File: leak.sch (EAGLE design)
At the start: 5 parts, among them IC1 74HC595D

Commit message: modifications
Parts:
- added C1, C2, C3, C4, C5, C6, C7, C8: 1uF, rcl:C-EUC0603
- added IC2, IC3: 74HC595D, 74xx-eu:74HC595D
- added U$10, U$5, U$6, U$7, U$8, U$9: AD5270MSOP10, untitled:AD5270MSOP10
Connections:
- new net +2V5: U$1.VDD, U$10.VDD, U$2.VDD, U$5.VDD, U$6.VDD, U$7.VDD, U$8.VDD, U$9.VDD
- new net -2V5: U$1.VSS, U$10.VSS, U$2.VSS, U$5.VSS, U$6.VSS, U$7.VSS, U$8.VSS, U$9.VSS
- new net AQA: IC1A.QA, U$2.A
- new net AQB: IC1A.QB, U$1.A
- new net AQC: IC1A.QC, U$5.A
- new net AQD: IC1A.QD, U$6.A
- new net AQE: IC1A.QE, U$7.A
- new net AQF: IC1A.QF, U$8.A
- new net AQG: IC1A.QG, U$9.A
- new net AQH: IC1A.QH, U$10.A
- new net CSA: IC2A.QA, U$2.NSYNC
- new net CSB: IC2A.QB, U$1.NSYNC
- new net CSC: IC2A.QC, U$5.NSYNC
- new net CSD: IC2A.QD, U$6.NSYNC
- new net CSE: IC2A.QE, U$7.NSYNC
- new net CSF: IC2A.QF, U$8.NSYNC
- new net CSG: IC2A.QG, U$9.NSYNC
- new net CSH: IC2A.QH, U$10.NSYNC
- new net GND: C1.1, C2.1, C3.1, C4.1, C5.1, C6.1, C7.1, C8.1, U$1.GND, U$10.GND, U$2.GND, U$5.GND, U$6.GND, U$7.GND, U$8.GND, U$9.GND
- new net MISO: U$1.SDO, U$10.SDO, U$2.SDO, U$5.SDO, U$6.SDO, U$7.SDO, U$8.SDO, U$9.SDO
- new net MOSI: U$1.DIN, U$10.DIN, U$2.DIN, U$5.DIN, U$6.DIN, U$7.DIN, U$8.DIN, U$9.DIN
- new net N$11: C4.2, U$6.CAP
- new net N$14: C5.2, U$7.CAP
- new net N$17: C6.2, U$8.CAP
- new net N$20: C7.2, U$9.CAP
- new net N$23: C8.2, U$10.CAP
- new net N$3: C2.2, U$1.CAP
- new net N$5: C1.2, U$2.CAP
- new net N$8: C3.2, U$5.CAP
- new net SCLK: U$1.SCLK, U$10.SCLK, U$2.SCLK, U$5.SCLK, U$6.SCLK, U$7.SCLK, U$8.SCLK, U$9.SCLK
- new net W: U$1.W, U$10.W, U$2.W, U$5.W, U$6.W, U$7.W, U$8.W, U$9.W
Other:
- moved on the sheet: IC1, U$1, U$3

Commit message: few more connections
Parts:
- removed C8: 1uF, rcl:C-EUC0603
- removed IC3: 74HC595D, 74xx-eu:74HC595D
- removed U$1, U$10, U$2, U$5, U$6, U$7, U$8, U$9: AD5270MSOP10, untitled:AD5270MSOP10
- removed U$3: AD5231, untitled:AD5231
- removed U$4: ADG621, untitled:ADG621
- added ICA, ICB, ICC, ICD, ICE, ICF, ICG: AD5270MSOP10, untitled:AD5270MSOP10
- added ICPOW: AD5231, untitled:AD5231
- added ICSW: ADG621, untitled:ADG621
- added JP1: (no value), pinhead:PINHD-1X3
- added JP4: (no value), pinhead:PINHD-1X6
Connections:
- removed net N$23: C8.2, U$10.CAP
- new net +5V: ICSW.VDD, JP1.1
- new net -5V: ICSW.VSS, JP1.3
- new net CS_CS: IC2A.RCK, JP4.2
- new net CS_IN: IC1A.RCK, JP4.1
- new net LVLA: ICPOW.A, ICSW.D1
- new net LVLB: ICPOW.B, ICSW.D2
- new net LVLW: ICPOW.W
- new net O1: ICPOW.O1, ICSW.IN1
- new net O2: ICPOW.O2, ICSW.IN2
- new net RESET: IC1A.SCL, IC2A.SCL
- net +2V5: now also IC1P.VCC, IC2P.VCC, ICA.VDD, ICB.VDD, ICC.VDD, ICD.VDD, ICE.VDD, ICF.VDD, ICG.VDD, ICPOW.NPR, ICPOW.NWP, ICPOW.VDD, ICSW.S2; no longer U$1.VDD, U$10.VDD, U$2.VDD, U$5.VDD, U$6.VDD, U$7.VDD, U$8.VDD, U$9.VDD
- net -2V5: now also ICA.VSS, ICB.VSS, ICC.VSS, ICD.VSS, ICE.VSS, ICF.VSS, ICG.VSS, ICPOW.T, ICPOW.VSS, ICSW.S1; no longer U$1.VSS, U$10.VSS, U$2.VSS, U$5.VSS, U$6.VSS, U$7.VSS, U$8.VSS, U$9.VSS
- net AQA: now also ICA.A; no longer U$2.A
- net AQB: now also ICB.A; no longer U$1.A
- net AQC: now also ICC.A; no longer U$5.A
- net AQD: now also ICD.A; no longer U$6.A
- net AQE: now also ICE.A; no longer U$7.A
- net AQF: now also ICF.A; no longer U$8.A
- net AQG: now also ICG.A; no longer U$9.A
- net AQH: no longer U$10.A
- net CSA: now also ICA.NSYNC; no longer U$2.NSYNC
- net CSB: now also ICB.NSYNC; no longer U$1.NSYNC
- net CSC: now also ICC.NSYNC; no longer U$5.NSYNC
- net CSD: now also ICD.NSYNC; no longer U$6.NSYNC
- net CSE: now also ICE.NSYNC; no longer U$7.NSYNC
- net CSF: now also ICF.NSYNC; no longer U$8.NSYNC
- net CSG: now also ICG.NSYNC; no longer U$9.NSYNC
- net CSH: now also ICPOW.NCS; no longer U$10.NSYNC
- net GND: now also IC1A.G, IC1P.GND, IC2A.G, IC2P.GND, ICA.GND, ICB.GND, ICC.GND, ICD.GND, ICE.GND, ICF.GND, ICG.GND, ICPOW.GND, ICSW.GND, JP1.2, JP4.6; no longer C8.1, U$1.GND, U$10.GND, U$2.GND, U$5.GND, U$6.GND, U$7.GND, U$8.GND, U$9.GND
- net MISO: now also ICA.SDO, ICB.SDO, ICC.SDO, ICD.SDO, ICE.SDO, ICF.SDO, ICG.SDO, ICPOW.SDO, JP4.4; no longer U$1.SDO, U$10.SDO, U$2.SDO, U$5.SDO, U$6.SDO, U$7.SDO, U$8.SDO, U$9.SDO
- net MOSI: now also IC1A.SER, IC2A.SER, ICA.DIN, ICB.DIN, ICC.DIN, ICD.DIN, ICE.DIN, ICF.DIN, ICG.DIN, ICPOW.SDI, JP4.3; no longer U$1.DIN, U$10.DIN, U$2.DIN, U$5.DIN, U$6.DIN, U$7.DIN, U$8.DIN, U$9.DIN
- net N$11: now also ICD.CAP; no longer U$6.CAP
- net N$14: now also ICE.CAP; no longer U$7.CAP
- net N$17: now also ICF.CAP; no longer U$8.CAP
- net N$20: now also ICG.CAP; no longer U$9.CAP
- net N$3: now also ICB.CAP; no longer U$1.CAP
- net N$5: now also ICA.CAP; no longer U$2.CAP
- net N$8: now also ICC.CAP; no longer U$5.CAP
- net SCLK: now also IC1A.SCK, IC2A.SCK, ICA.SCLK, ICB.SCLK, ICC.SCLK, ICD.SCLK, ICE.SCLK, ICF.SCLK, ICG.SCLK, ICPOW.CLK, JP4.5; no longer U$1.SCLK, U$10.SCLK, U$2.SCLK, U$5.SCLK, U$6.SCLK, U$7.SCLK, U$8.SCLK, U$9.SCLK
- net W: now also ICA.W, ICB.W, ICC.W, ICD.W, ICE.W, ICF.W, ICG.W; no longer U$1.W, U$10.W, U$2.W, U$5.W, U$6.W, U$7.W, U$8.W, U$9.W
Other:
- moved on the sheet: C1, C2, C3, C4, C5, C6, C7, IC1, IC1P, IC2

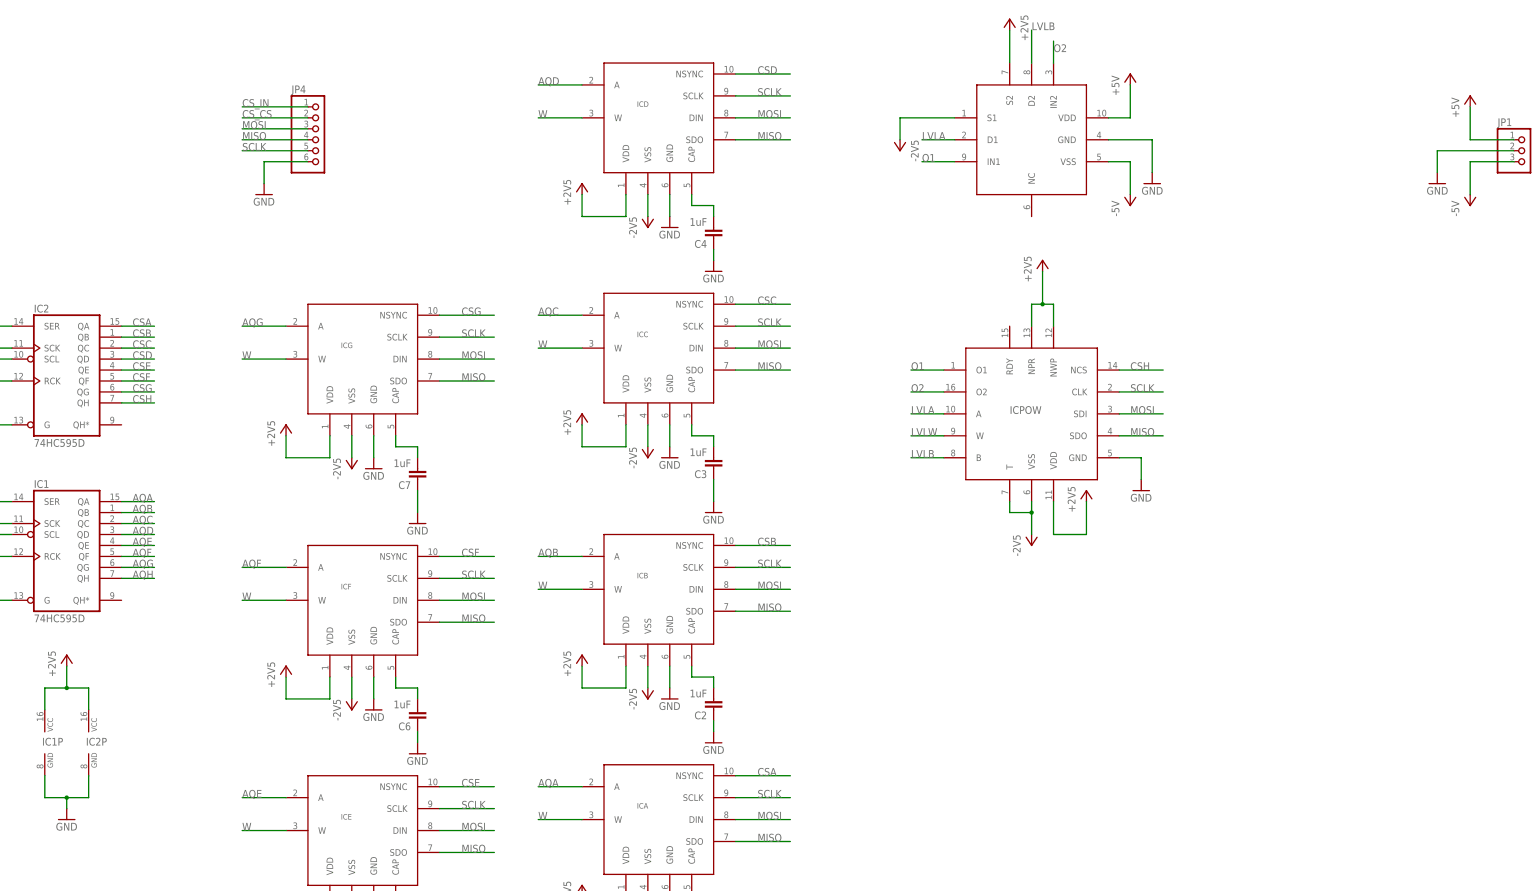
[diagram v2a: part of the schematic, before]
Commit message: added link to a viewer and op amp
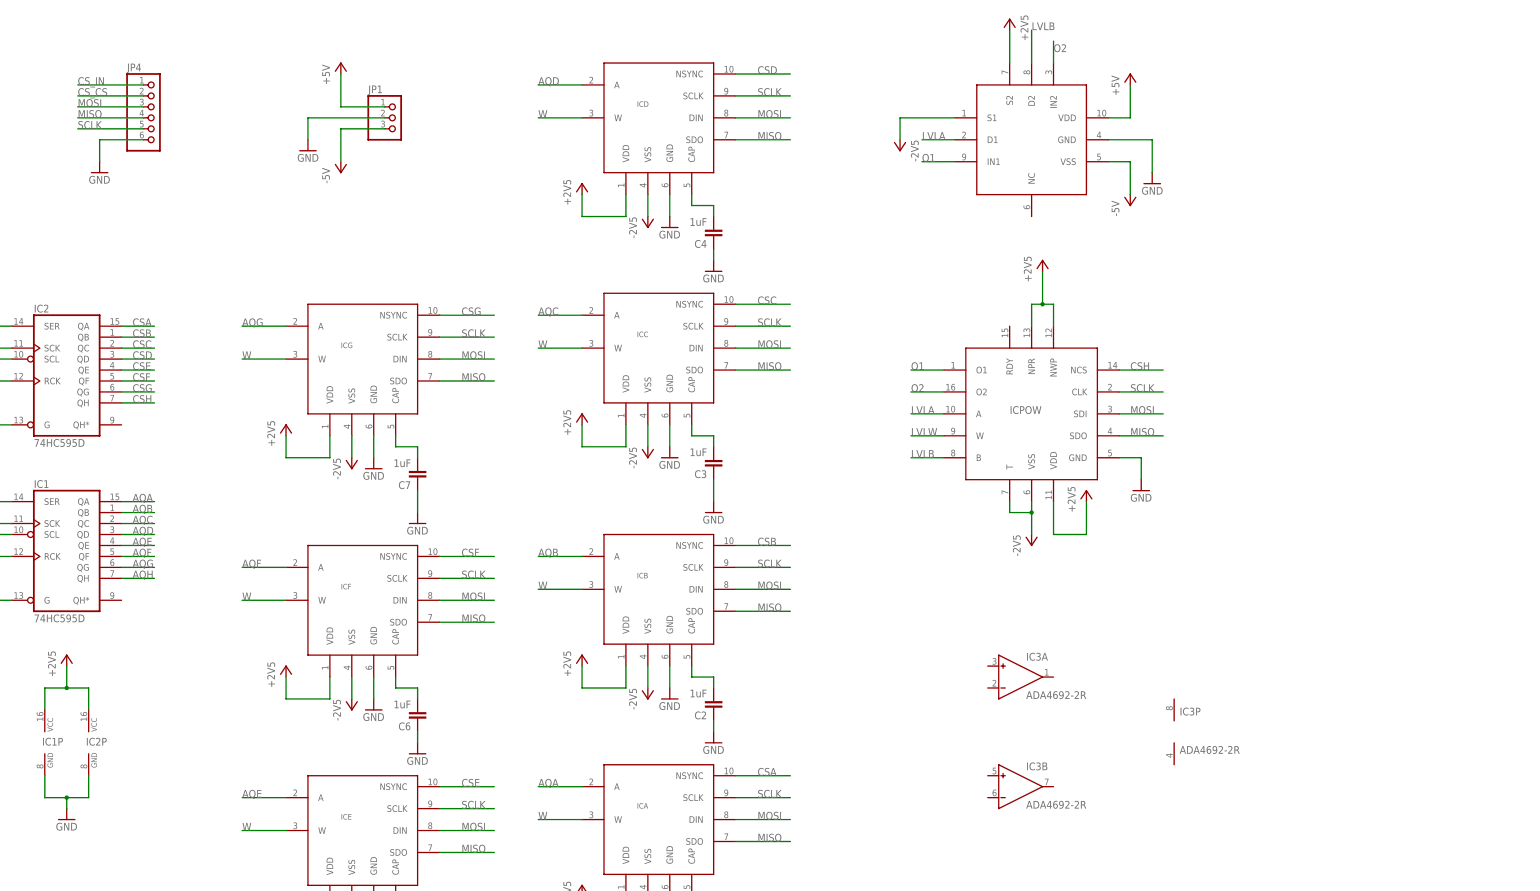
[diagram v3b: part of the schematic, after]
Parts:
- added IC3: ADA4692-2R, analog-devices:ADA4692-2R
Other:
- moved on the sheet: JP1, JP4
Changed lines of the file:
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@@
 <part name="GND21" library="supply1" library_urn="urn:adsk.eagle:library:371" deviceset="GND" device=""/>
 <part name="JP4" library="pinhead" library_urn="urn:adsk.eagle:library:325" deviceset="PINHD-1X6" device="" package3d_urn="urn:adsk.eagle:package:22472/2"/>
+<part name="IC3" library="analog-devices" library_urn="urn:adsk.eagle:library:102" deviceset="ADA4692-2" device="R" package3d_urn="urn:adsk.eagle:package:30987/2"/>
 </parts>
 <sheets>
@@
 <attribute name="VALUE" x="40.64" y="99.06" size="1.778" layer="96" rot="MR0"/>
 </instance>
-<instance part="JP1" gate="A" x="396.24" y="213.36" smashed="yes">
-<attribute name="NAME" x="389.89" y="219.075" size="1.778" layer="95"/>
-<attribute name="VALUE" x="389.89" y="205.74" size="1.778" layer="96"/>
-</instance>
-<instance part="P+1" gate="1" x="383.54" y="226.06" smashed="yes">
-<attribute name="VALUE" x="381" y="220.98" size="1.778" layer="96" rot="R90"/>
-</instance>
-<instance part="P-11" gate="1" x="383.54" y="200.66" smashed="yes">
-<attribute name="VALUE" x="381" y="198.12" size="1.778" layer="96" rot="R90"/>
-</instance>
-<instance part="GND20" gate="1" x="375.92" y="205.74" smashed="yes" rot="MR0">
-<attribute name="VALUE" x="378.46" y="203.2" size="1.778" layer="96" rot="MR0"/>
+<instance part="JP1" gate="A" x="134.62" y="220.98" smashed="yes">
+<attribute name="NAME" x="128.27" y="226.695" size="1.778" layer="95"/>
+<attribute name="VALUE" x="128.27" y="213.36" size="1.778" layer="96"/>
+</instance>
+<instance part="P+1" gate="1" x="121.92" y="233.68" smashed="yes">
+<attribute name="VALUE" x="119.38" y="228.6" size="1.778" layer="96" rot="R90"/>
+</instance>
+<instance part="P-11" gate="1" x="121.92" y="208.28" smashed="yes">
+<attribute name="VALUE" x="119.38" y="205.74" size="1.778" layer="96" rot="R90"/>
+</instance>
+<instance part="GND20" gate="1" x="114.3" y="213.36" smashed="yes" rot="MR0">
+<attribute name="VALUE" x="116.84" y="210.82" size="1.778" layer="96" rot="MR0"/>
 </instance>
 <instance part="P+2" gate="1" x="304.8" y="231.14" smashed="yes">
@@
 <attribute name="VALUE" x="302.26" y="198.12" size="1.778" layer="96" rot="R90"/>
 </instance>
-<instance part="GND21" gate="1" x="104.14" y="203.2" smashed="yes">
-<attribute name="VALUE" x="101.6" y="200.66" size="1.778" layer="96"/>
-</instance>
-<instance part="JP4" gate="A" x="116.84" y="215.9" smashed="yes">
-<attribute name="NAME" x="110.49" y="226.695" size="1.778" layer="95"/>
-<attribute name="VALUE" x="110.49" y="205.74" size="1.778" layer="96"/>
+<instance part="GND21" gate="1" x="66.04" y="208.28" smashed="yes">
+<attribute name="VALUE" x="63.5" y="205.74" size="1.778" layer="96"/>
+</instance>
+<instance part="JP4" gate="A" x="78.74" y="220.98" smashed="yes">
+<attribute name="NAME" x="72.39" y="231.775" size="1.778" layer="95"/>
+<attribute name="VALUE" x="72.39" y="210.82" size="1.778" layer="96"/>
 </instance>
 <instance part="IC2" gate="P" x="63.5" y="76.2" smashed="yes">
 <attribute name="NAME" x="62.865" y="75.565" size="1.778" layer="95"/>
+</instance>
+<instance part="IC3" gate="A" x="276.86" y="91.44" smashed="yes">
+<attribute name="NAME" x="280.67" y="95.25" size="1.778" layer="95"/>
+<attribute name="VALUE" x="280.67" y="86.36" size="1.778" layer="96"/>
+</instance>
+<instance part="IC3" gate="B" x="276.86" y="66.04" smashed="yes">
+<attribute name="NAME" x="280.67" y="69.85" size="1.778" layer="95"/>
+<attribute name="VALUE" x="280.67" y="60.96" size="1.778" layer="96"/>
+</instance>
+<instance part="IC3" gate="P" x="314.96" y="78.74" smashed="yes">
+<attribute name="NAME" x="316.23" y="82.55" size="1.778" layer="95"/>
+<attribute name="VALUE" x="316.23" y="73.66" size="1.778" layer="96"/>
 </instance>
 </instances>
@@
 <segment>
 <pinref part="JP4" gate="A" pin="5"/>
-<wire x1="114.3" y1="213.36" x2="99.06" y2="213.36" width="0.1524" layer="91"/>
-<label x="99.06" y="213.36" size="1.778" layer="95"/>
+<wire x1="76.2" y1="218.44" x2="60.96" y2="218.44" width="0.1524" layer="91"/>
+<label x="60.96" y="218.44" size="1.778" layer="95"/>
 </segment>
 </net>
@@
 <segment>
 <pinref part="JP4" gate="A" pin="3"/>
-<wire x1="114.3" y1="218.44" x2="99.06" y2="218.44" width="0.1524" layer="91"/>
-<label x="99.06" y="218.44" size="1.778" layer="95"/>
+<wire x1="76.2" y1="223.52" x2="60.96" y2="223.52" width="0.1524" layer="91"/>
+<label x="60.96" y="223.52" size="1.778" layer="95"/>
 </segment>
 </net>
@@
 <segment>
 <pinref part="JP4" gate="A" pin="4"/>
-<wire x1="114.3" y1="215.9" x2="99.06" y2="215.9" width="0.1524" layer="91"/>
-<label x="99.06" y="215.9" size="1.778" layer="95"/>
+<wire x1="76.2" y1="220.98" x2="60.96" y2="220.98" width="0.1524" layer="91"/>
+<label x="60.96" y="220.98" size="1.778" layer="95"/>
 </segment>
 </net>
@@
 <segment>
 <pinref part="JP1" gate="A" pin="2"/>
-<wire x1="393.7" y1="213.36" x2="375.92" y2="213.36" width="0.1524" layer="91"/>
-<wire x1="375.92" y1="213.36" x2="375.92" y2="208.28" width="0.1524" layer="91"/>
+<wire x1="132.08" y1="220.98" x2="114.3" y2="220.98" width="0.1524" layer="91"/>
+<wire x1="114.3" y1="220.98" x2="114.3" y2="215.9" width="0.1524" layer="91"/>
 <pinref part="GND20" gate="1" pin="GND"/>
 </segment>
 <segment>
 <pinref part="GND21" gate="1" pin="GND"/>
-<wire x1="104.14" y1="205.74" x2="104.14" y2="210.82" width="0.1524" layer="91"/>
+<wire x1="66.04" y1="210.82" x2="66.04" y2="215.9" width="0.1524" layer="91"/>
 <pinref part="JP4" gate="A" pin="6"/>
-<wire x1="114.3" y1="210.82" x2="104.14" y2="210.82" width="0.1524" layer="91"/>
+<wire x1="76.2" y1="215.9" x2="66.04" y2="215.9" width="0.1524" layer="91"/>
 </segment>
 </net>
@@
 <segment>
 <pinref part="JP4" gate="A" pin="2"/>
-<wire x1="114.3" y1="220.98" x2="99.06" y2="220.98" width="0.1524" layer="91"/>
-<label x="99.06" y="220.98" size="1.778" layer="95"/>
+<wire x1="76.2" y1="226.06" x2="60.96" y2="226.06" width="0.1524" layer="91"/>
+<label x="60.96" y="226.06" size="1.778" layer="95"/>
 </segment>
 </net>
@@
 <segment>
 <pinref part="JP4" gate="A" pin="1"/>
-<wire x1="114.3" y1="223.52" x2="99.06" y2="223.52" width="0.1524" layer="91"/>
-<label x="99.06" y="223.52" size="1.778" layer="95"/>
+<wire x1="76.2" y1="228.6" x2="60.96" y2="228.6" width="0.1524" layer="91"/>
+<label x="60.96" y="228.6" size="1.778" layer="95"/>
 </segment>
 </net>
@@
 <segment>
 <pinref part="JP1" gate="A" pin="3"/>
-<wire x1="393.7" y1="210.82" x2="383.54" y2="210.82" width="0.1524" layer="91"/>
-<wire x1="383.54" y1="210.82" x2="383.54" y2="203.2" width="0.1524" layer="91"/>
+<wire x1="132.08" y1="218.44" x2="121.92" y2="218.44" width="0.1524" layer="91"/>
+<wire x1="121.92" y1="218.44" x2="121.92" y2="210.82" width="0.1524" layer="91"/>
 <pinref part="P-11" gate="1" pin="-5V"/>
 </segment>
@@
 <segment>
 <pinref part="JP1" gate="A" pin="1"/>
-<wire x1="393.7" y1="215.9" x2="383.54" y2="215.9" width="0.1524" layer="91"/>
-<wire x1="383.54" y1="215.9" x2="383.54" y2="223.52" width="0.1524" layer="91"/>
+<wire x1="132.08" y1="223.52" x2="121.92" y2="223.52" width="0.1524" layer="91"/>
+<wire x1="121.92" y1="223.52" x2="121.92" y2="231.14" width="0.1524" layer="91"/>
 <pinref part="P+1" gate="1" pin="+5V"/>
 </segment>

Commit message: finished schematic
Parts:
- added C10: 10nF, rcl:C-EUC0603
- added C11, C12: 2uF, rcl:C-EUC0603
- added C13: 2uF, rcl:C-EUC0805K
- added C8, C9: 1uF, rcl:C-EUC0603
- added R1: 1M, rcl:R-EU_R0805
- added R2: 10K, rcl:R-EU_R0805
- added R3: 4.7K, rcl:R-EU_R0805
- added U$1: TLV703, titled:TLV703
- added U1: TPS72301DBVRSOT-23-5, titled:TPS72301DBVRSOT-23-5
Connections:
- new net N$1: C10.2, U1.FB
- new net N$2: IC3A.OUT, IC3B.IN+, R2.2, R3.2
- new net N$4: IC3B.OUT
- new net N$6: IC3A.IN-, R1.2, R2.1
- net +2V5: now also C12.2, IC3P.V+, U$1.OUT
- net +5V: now also C11.2, U$1.EN, U$1.IN
- net -2V5: now also C8.2, IC3P.V-, U1.OUT
- net -5V: now also C9.2, U1.EN, U1.IN
- net GND: now also C10.1, C11.1, C12.1, C13.2, C8.1, C9.1, R1.1, U$1.GND, U1.GND
- net LVLW: now also IC3B.IN-
- net W: now also C13.1, IC3A.IN+, R3.1
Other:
- moved on the sheet: C1, C2, C3, C4, C5, C6, C7, IC1, IC1P, IC2, IC2P, IC3A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

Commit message: started pcb layout
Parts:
- added IC4: ADA4692-2R, analog-devices:ADA4692-2R
- added JP2: (no value), pinhead:PINHD-1X1
- added LED+2.5, LED-2.5, LED_OUT+, LED_OUT-, LED_OUT-1: (no value), led:LEDCHIPLED_0805
- added R4, R5, R6, R7, R8: 200, rcl:R-EU_R0603
- renumbered ICA to ICH, U$1 to U2
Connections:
- removed net RESET: IC1A.SCL, IC2A.SCL
- new net N$10: LED_OUT-.A, R7.2
- new net N$12: LED_OUT-1.C, R8.2
- new net N$7: LED+2.5.C, R5.2
- new net N$9: LED_OUT+.C, R6.2
- new net OUT: IC3B.OUT, IC4A.IN+, IC4A.IN-, IC4A.OUT, JP2.1, LED_OUT+.A, LED_OUT-.C, LED_OUT-1.A
- net +2V5: now also IC1A.SCL, IC2A.SCL, IC4P.V+, LED+2.5.A
- net -2V5: now also LED-2.5.C
- net AQA: no longer ICH.A
- net AQH: now also ICH.A
- net CSA: now also ICPOW.NCS; no longer ICH.NSYNC
- net CSH: now also ICH.NSYNC; no longer ICPOW.NCS
- net GND: now also IC4P.V-, R4.1, R5.1, R6.1, R7.1, R8.1
- net MISO: now also JP4.3; no longer JP4.4
- net MOSI: now also JP4.4; no longer JP4.3
- net N$4: now also LED-2.5.A, R4.2; no longer IC3B.OUT
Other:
- moved on the sheet: C13, IC3A, IC3B, R1, R2, R3

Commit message: v1 finished
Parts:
- renumbered LED_OUT+ to BIPOUT+, LED_OUT- to BIPOUT-, LED_OUT-1 to LEDOUT
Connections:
- removed net AQA: IC1A.QA
- new net OUT_BIP: BIPOUT+.A, BIPOUT-.C, IC3B.OUT, IC4A.IN+
- net +2V5: now also ICSW.VDD
- net +5V: no longer ICSW.VDD
- net -2V5: now also ICSW.VSS
- net -5V: no longer ICSW.VSS
- net OUT: no longer BIPOUT+.A, BIPOUT-.C, IC3B.OUT, IC4A.IN+
